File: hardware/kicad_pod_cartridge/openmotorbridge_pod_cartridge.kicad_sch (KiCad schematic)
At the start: 29 parts, among them Q1 AO3400A, Q2 AO3400A, Q3 AO3400A, Q4 AO3400A, U1 CH32V003F4P6, U3 ES8388

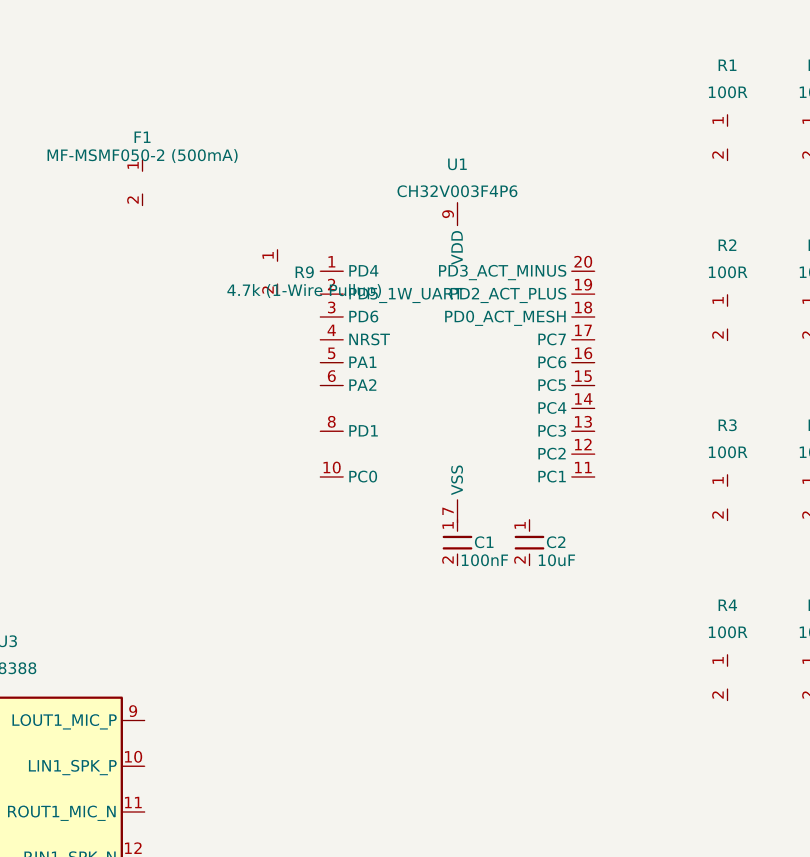
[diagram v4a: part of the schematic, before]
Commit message: feat(hw): finalize PCB lineup routing, sync PCBA 03 cartridge with J_PROG header and DTM12 schematics
- PCBA 01 (Central Box): Remediate net routing, DTM12 hierarchical schematic synchronization, 100% routed, 0 DRC errors.
- PCBA 03 (Smart Modular Cartridge): Position and route J_PROG 4-pin SMD programming header on F.Cu at (108.0, 89.61), synchronize CPL and schematic, 100% routed, 0 DRC errors.
- PCBA 05 (Universal Front Node): Preconnect and routing verified, 100% routed, 0 DRC errors.
- PCBA 07 (LoRa Smart-Keyfob): Routing and DRC verified, 100% routed, 0 DRC errors.
- PCBA 08 (Radar 2.0 Sub-MCU & Wings): Sub-MCU routing and HF isolation verified, 100% routed, 0 DRC errors.
- PCBA 10 (OMM 446 PMR/DMR Intercom): KiCad DRC verified, 100% routed, 0 DRC errors.
- Firmware: Align configuration headers across front_node and smart_cartridge.
- Tools: Add comprehensive preflight PCBA audit suite tools/audit_pcbas_preflight.py.
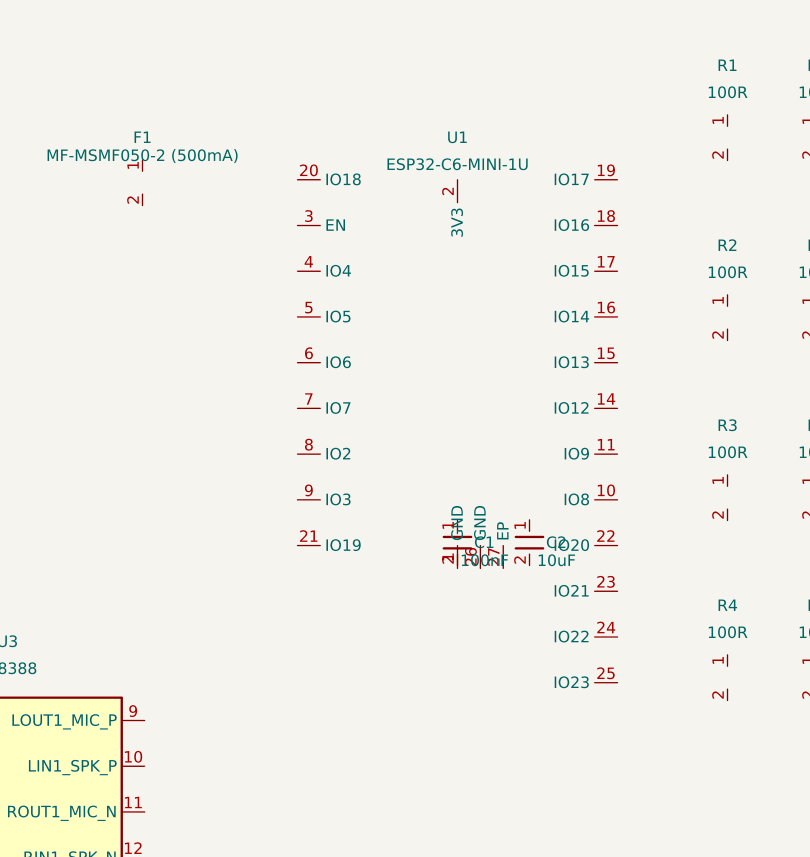
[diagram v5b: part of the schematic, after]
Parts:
- removed R9: 4.7k (1-Wire Pullup), Resistor_SMD:R_0603_1608Metric, symbol Device:R_Small
- added J_PROG: SWD_PROG_4P, Connector_PinHeader_1.27mm:PinHeader_1x04_P1.27mm_Vertical_SMD_Pin1Left, symbol Connector:Conn_01x04_SWD
- U1: value CH32V003F4P6 -> ESP32-C6-MINI-1U; footprint Package_SO:TSSOP-20_4.4x6.5mm_P0.65mm -> RF_Module:ESP32-C6-MINI-1U; symbol MCU_WCH:CH32V003F4P6 -> MCU:ESP32-C6-MINI-1U; LCSC C5248205 -> C5287747
- U_UWB: renamed from J_PROG; value SWD_PROG_4P -> DW3110; footprint Connector_PinHeader_1.27mm:PinHeader_1x04_P1.27mm_Vertical_SMD_Pin1Left -> Package_DFN_QFN:QFN-16-1EP_3x3mm_P0.5mm_EP1.7x1.7mm_ThermalVias; symbol Connector:Conn_01x04_SWD -> RF_Module:DW3110
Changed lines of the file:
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@@
 		(pin "2")
 	)
-	(symbol (lib_id "MCU_WCH:CH32V003F4P6") (at 110.0 75.0 0) (unit 1)
-		(in_bom yes) (on_board yes) (dnp no)
-		(property "Reference" "U1" (at 110.0 53.0 0) (effects (font (size 1.27 1.27))))
-		(property "Value" "CH32V003F4P6" (at 110.0 56.0 0) (effects (font (size 1.27 1.27))))
-		(property "Footprint" "Package_SO:TSSOP-20_4.4x6.5mm_P0.65mm" (at 0 0 0) (effects (font (size 1.27 1.27)) hide))
-		(property "LCSC" "C5248205" (at 0 0 0) (effects (font (size 1.27 1.27)) hide))
+	(symbol (lib_id "MCU:ESP32-C6-MINI-1U") (at 110.0 75.0 0) (unit 1)
+		(in_bom yes) (on_board yes) (dnp no)
+		(property "Reference" "U1" (at 110.0 50.0 0) (effects (font (size 1.27 1.27))))
+		(property "Value" "ESP32-C6-MINI-1U" (at 110.0 53.0 0) (effects (font (size 1.27 1.27))))
+		(property "Footprint" "RF_Module:ESP32-C6-MINI-1U" (at 0 0 0) (effects (font (size 1.27 1.27)) hide))
+		(property "LCSC" "C5287747" (at 0 0 0) (effects (font (size 1.27 1.27)) hide))
 		(pin "1")
 		(pin "2")
@@
 		(pin "10")
 		(pin "11")
-		(pin "12")
-		(pin "13")
 		(pin "14")
 		(pin "15")
@@
 		(pin "19")
 		(pin "20")
+		(pin "21")
+		(pin "22")
+		(pin "23")
+		(pin "24")
+		(pin "25")
+		(pin "26")
+		(pin "27")
 	)
 	(symbol (lib_id "Transistor_FET:AO3400A") (at 160.0 50.0 0) (unit 1)
@@
 		(property "Footprint" "Capacitor_SMD:C_0805_2012Metric" (at 0 0 0) (effects (font (size 1.27 1.27)) hide))
 		(property "LCSC" "C15850" (at 0 0 0) (effects (font (size 1.27 1.27)) hide))
-		(pin "1")
-		(pin "2")
-	)
-	(symbol (lib_id "Device:R_Small") (at 90.0 65.0 0) (unit 1)
-		(in_bom yes) (on_board yes) (dnp no)
-		(property "Reference" "R9" (at 93.0 65.0 0) (effects (font (size 1.27 1.27))))
-		(property "Value" "4.7k (1-Wire Pullup)" (at 93.0 67.0 0) (effects (font (size 1.27 1.27))))
-		(property "Footprint" "Resistor_SMD:R_0603_1608Metric" (at 0 0 0) (effects (font (size 1.27 1.27)) hide))
-		(property "LCSC" "C23162" (at 0 0 0) (effects (font (size 1.27 1.27)) hide))
 		(pin "1")
 		(pin "2")
@@
 		(property "Value" "SWD_PROG_4P" (at 210.0 138.0 0) (effects (font (size 1.27 1.27))))
 		(property "Footprint" "Connector_PinHeader_1.27mm:PinHeader_1x04_P1.27mm_Vertical_SMD_Pin1Left" (at 0 0 0) (effects (font (size 1.27 1.27)) hide))
-		(pin "1")
-		(pin "2")
+		(property "LCSC" "C2957448" (at 0 0 0) (effects (font (size 1.27 1.27)) hide))
+		(pin "1")
+		(pin "2")

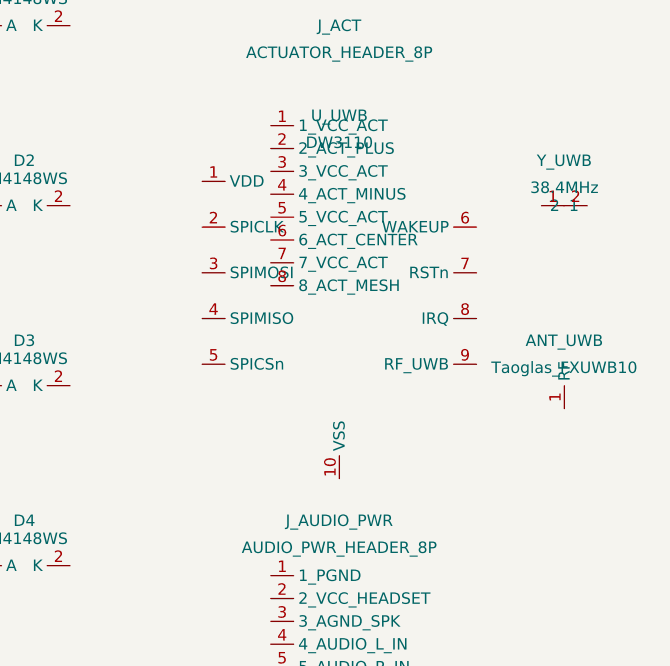
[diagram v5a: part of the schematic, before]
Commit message: fix(cartridge): wire Y_UWB crystal to DW3110 and unify PAD1 +5V_IN net
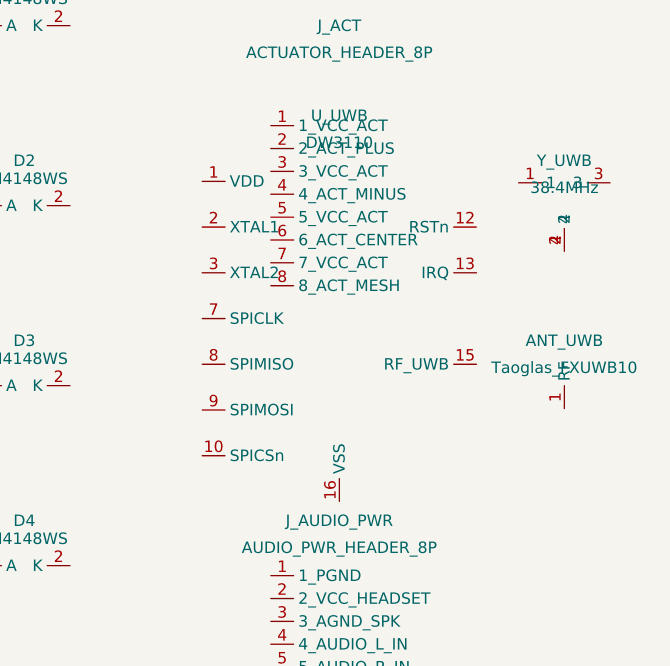
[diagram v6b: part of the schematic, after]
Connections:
- net at Y_UWB.2: now also Y_UWB.4
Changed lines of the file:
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@@
 		(pin "2")
 		(pin "3")
-		(pin "4")
-		(pin "5")
-		(pin "6")
 		(pin "7")
 		(pin "8")
 		(pin "9")
 		(pin "10")
+		(pin "12")
+		(pin "13")
+		(pin "15")
+		(pin "16")
 	)
 	(symbol (lib_id "Device:Crystal_Small") (at 235.0 70.0 0) (unit 1)
@@
 		(pin "1")
 		(pin "2")
+		(pin "3")
+		(pin "4")
 	)
 	(symbol (lib_id "Device:Antenna") (at 235.0 90.0 0) (unit 1)

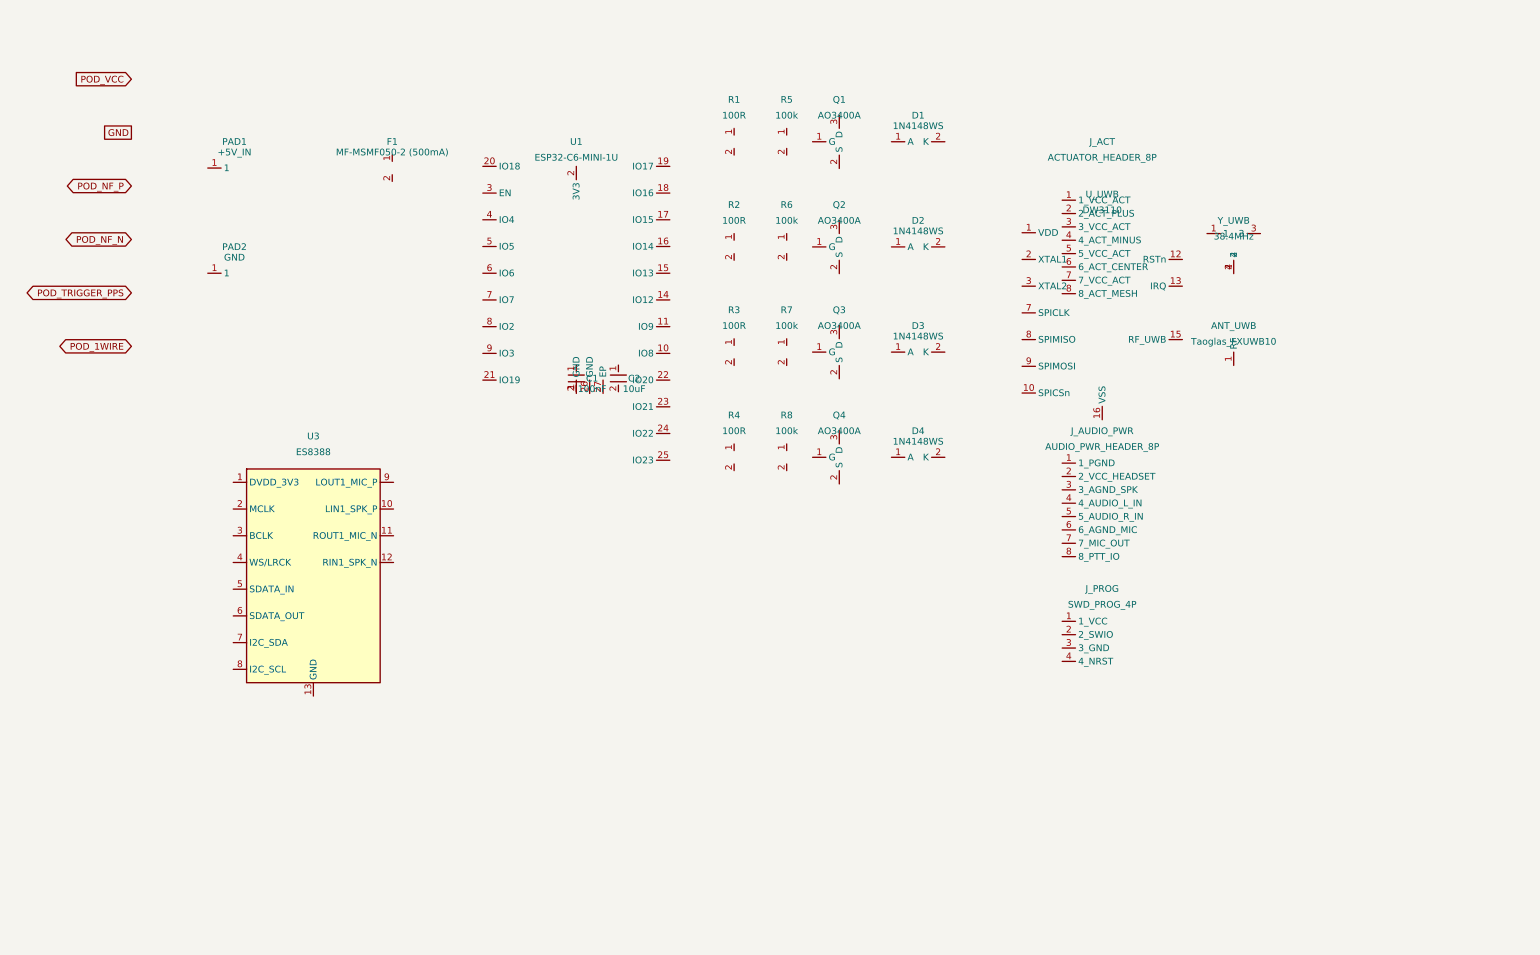
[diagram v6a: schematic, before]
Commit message: feat(hardware): achieve 100% 0-error DRC across all 7 official PCBAs and complete 4-layer Cartridge audio switching
- PCBA 01 (Central Box): Resolved keepout zone violation at U.FL ANT1, refilled zones (0 errors, 0 unconnected).
- PCBA 03 (Universal Smart Cartridge): Upgraded to 4 layers (JLC04161H), added SPDT analog/digital switch U4 (TS5A3159DBVR) on B.Cu and 10k pull-up R9 on F.Cu, routed symmetrical audio/OMM nets, schematic ERC 0 errors, DRC 0 errors, 0 unconnected.
- PCBA 05 (Front Node): 4-layer upgrade, solid GND plane, snapped OTTOCAST_FAULT_N (0 errors, 0 unconnected).
- PCBA 07 (Smart Keyfob): 4-layer upgrade, fixed Edge.Cuts arc alignment, routed U2 pad 23 (0 errors, 0 unconnected).
- PCBA 08 (Radar Sub-MCU), PCBA 09 (OMM 2.4 GHz), PCBA 10 (OMM 446 MHz): Verified 100% clean (0 errors, 0 unconnected).
- Added reproducibility tools: tools/sync_cartridge_sch.py and tools/remediate_pcba03.py.
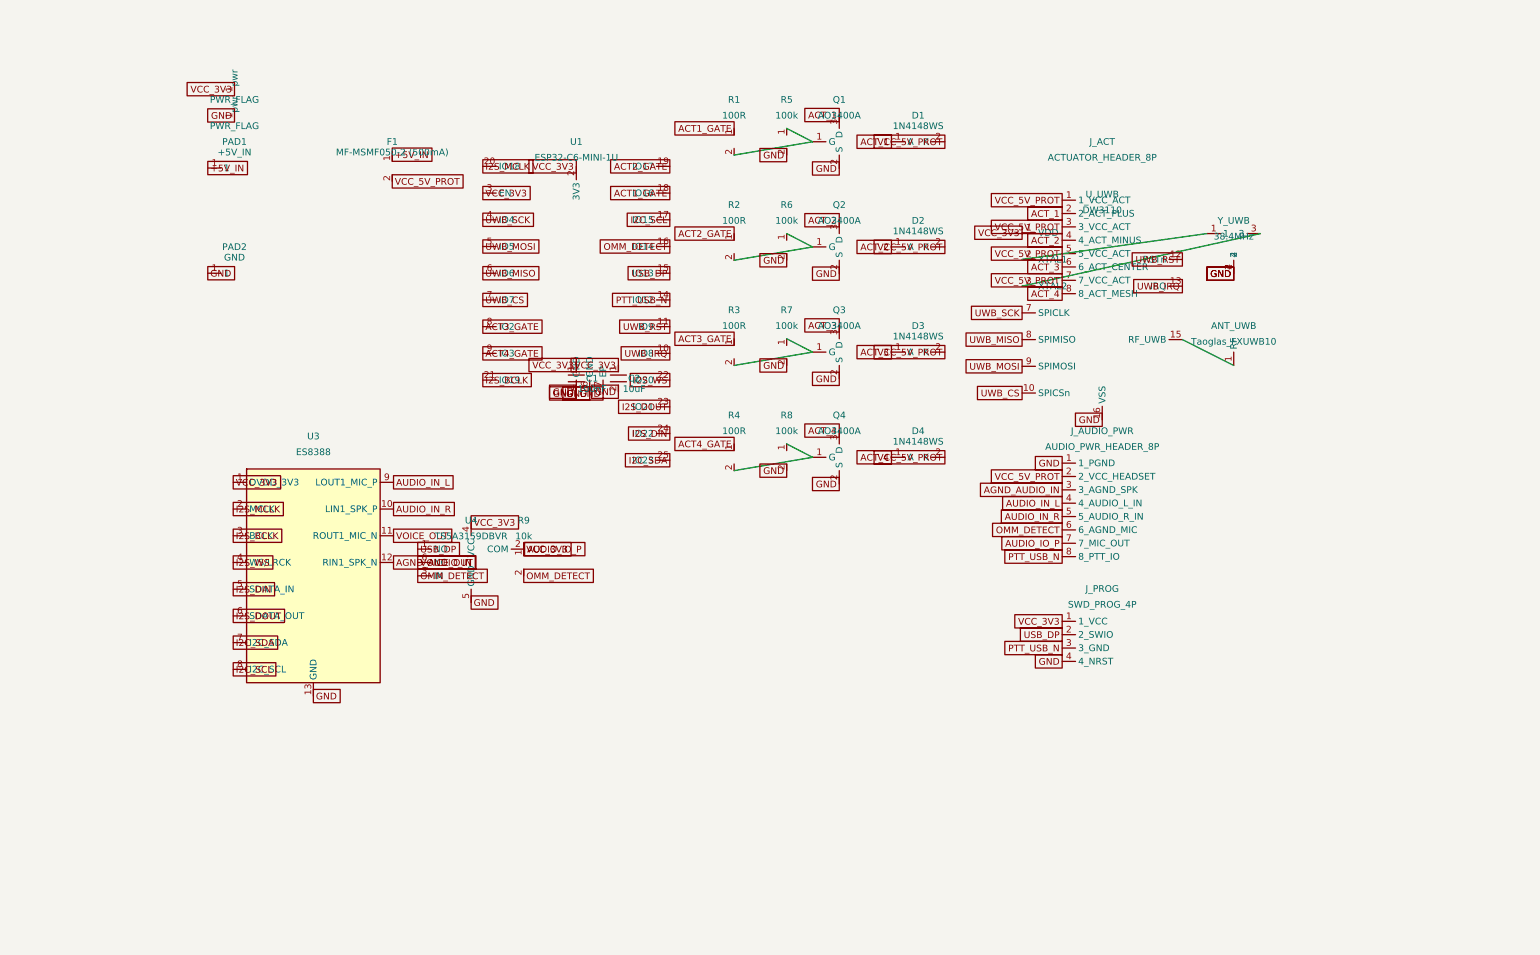
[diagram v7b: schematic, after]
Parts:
- added R9: 10k, Resistor_SMD:R_0603_1608Metric, symbol Device:R_Small
- added U4: TS5A3159DBVR, Package_TO_SOT_SMD:SOT-23-6, symbol Switch:TS5A3159_SPDT
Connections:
- net GND: now also C1.2, C2.2, J_AUDIO_PWR.1 (1_PGND), J_PROG.4 (4_NRST), PAD2.1, Q1.2 (S), Q2.2 (S), Q3.2 (S), Q4.2 (S), R5.2, R6.2, R7.2, R8.2, U1.1 (GND), U1.26 (GND), U1.27 (EP), U3.13 (GND), U_UWB.16 (VSS), Y_UWB.2, Y_UWB.4, U4.5 (GND)
- net +5V_IN: now reaches PAD1.1
- net +5V_IN: now also F1.1
- net VCC_5V_PROT: now reaches F1.2
- net VCC_5V_PROT: now also D1.2 (K), D2.2 (K), D3.2 (K), D4.2 (K), J_ACT.1 (1_VCC_ACT), J_ACT.3 (3_VCC_ACT), J_ACT.5 (5_VCC_ACT), J_ACT.7 (7_VCC_ACT), J_AUDIO_PWR.2 (2_VCC_HEADSET)
- net UWB_IRQ: now reaches U1.10 (IO8)
- net UWB_IRQ: now also U_UWB.13 (IRQ)
- net UWB_RST: now reaches U1.11 (IO9)
- net UWB_RST: now also U_UWB.12 (RSTn)
- net PTT_USB_N: now reaches U1.14 (IO12)
- net PTT_USB_N: now also J_AUDIO_PWR.8 (8_PTT_IO), J_PROG.3 (3_GND)
- net USB_DP: now reaches U1.15 (IO13)
- net USB_DP: now also J_PROG.2 (2_SWIO), U4.1 (NO)
- net OMM_DETECT: now reaches U1.16 (IO14)
- net OMM_DETECT: now also J_AUDIO_PWR.6 (6_AGND_MIC), R9.2, U4.3 (IN)
- net I2C_SCL: now reaches U1.17 (IO15)
- net I2C_SCL: now also U3.8 (I2C_SCL)
- net ACT1_GATE: now reaches U1.18 (IO16)
- net ACT1_GATE: now also R1.1
- net ACT2_GATE: now reaches U1.19 (IO17)
- net ACT2_GATE: now also R2.1
- net VCC_3V3: now reaches U1.2 (3V3)
- net VCC_3V3: now also C1.1, C2.1, J_PROG.1 (1_VCC), U1.3 (EN), U3.1 (DVDD_3V3), U_UWB.1 (VDD), R9.1, U4.4 (VCC)
- net I2S_MCLK: now reaches U1.20 (IO18)
- net I2S_MCLK: now also U3.2 (MCLK)
- net I2S_BCLK: now reaches U1.21 (IO19)
- net I2S_BCLK: now also U3.3 (BCLK)
- net I2S_WS: now reaches U1.22 (IO20)
- net I2S_WS: now also U3.4 (WS/LRCK)
- net I2S_DOUT: now reaches U1.23 (IO21)
- net I2S_DOUT: now also U3.6 (SDATA_OUT)
- net I2S_DIN: now reaches U1.24 (IO22)
- net I2S_DIN: now also U3.5 (SDATA_IN)
- net I2C_SDA: now reaches U1.25 (IO23)
- net I2C_SDA: now also U3.7 (I2C_SDA)
- net UWB_SCK: now reaches U1.4 (IO4)
- net UWB_SCK: now also U_UWB.7 (SPICLK)
- net UWB_MOSI: now reaches U1.5 (IO5)
- net UWB_MOSI: now also U_UWB.9 (SPIMOSI)
- net UWB_MISO: now reaches U1.6 (IO6)
- net UWB_MISO: now also U_UWB.8 (SPIMISO)
- net UWB_CS: now reaches U1.7 (IO7)
- net UWB_CS: now also U_UWB.10 (SPICSn)
- net ACT3_GATE: now reaches U1.8 (IO2)
- net ACT3_GATE: now also R3.1
- net ACT4_GATE: now reaches U1.9 (IO3)
- net ACT4_GATE: now also R4.1
- net at Q1.1 (G): now also R1.2, R5.1
- net ACT_1: now reaches Q1.3 (D)
- net ACT_1: now also D1.1 (A), J_ACT.2 (2_ACT_PLUS)
- net at Q2.1 (G): now also R2.2, R6.1
- net ACT_2: now reaches Q2.3 (D)
- net ACT_2: now also D2.1 (A), J_ACT.4 (4_ACT_MINUS)
- net at Q3.1 (G): now also R3.2, R7.1
- net ACT_3: now reaches Q3.3 (D)
- net ACT_3: now also D3.1 (A), J_ACT.6 (6_ACT_CENTER)
- net at Q4.1 (G): now also R4.2, R8.1
- net ACT_4: now reaches Q4.3 (D)
- net ACT_4: now also D4.1 (A), J_ACT.8 (8_ACT_MESH)
- net AGND_AUDIO_IN: now reaches J_AUDIO_PWR.3 (3_AGND_SPK)
- net AGND_AUDIO_IN: now also U3.12 (RIN1_SPK_N)
- net AUDIO_IN_L: now reaches J_AUDIO_PWR.4 (4_AUDIO_L_IN)
- net AUDIO_IN_L: now also U3.9 (LOUT1_MIC_P)
- net AUDIO_IN_R: now reaches J_AUDIO_PWR.5 (5_AUDIO_R_IN)
- net AUDIO_IN_R: now also U3.10 (LIN1_SPK_P)
- net AUDIO_IO_P: now reaches J_AUDIO_PWR.7 (7_MIC_OUT)
- net AUDIO_IO_P: now also U4.2 (COM)
- net at U_UWB.15 (RF_UWB): now also ANT_UWB.1 (RF)
- net at U_UWB.2 (XTAL1): now also Y_UWB.1
- net at U_UWB.3 (XTAL2): now also Y_UWB.3
- net VOICE_OUT: now reaches U3.11 (ROUT1_MIC_N)
- net VOICE_OUT: now also U4.6 (NC)
